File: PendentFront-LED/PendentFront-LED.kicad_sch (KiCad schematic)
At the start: 64 parts, among them J1 Conn_01x04_Pin, U1 74VHC9595FT, U2 74VHC9595FT, U3 74VHC9595FT

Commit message: Finalized pendent shape and started routing
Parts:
- removed J1: Conn_01x04_Pin, Connector_PinHeader_2.54mm:PinHeader_1x04_P2.54mm_Vertical, symbol Connector:Conn_01x04_Pin
- removed LED10, LED11, LED12, LED13, LED14, LED15, LED16, LED17, LED18, LED19, LED20, LED21, LED22, LED23, LED24, LED25, LED26, LED27, LED28, LED29, LED3, LED30, LED31, LED32, LED33, LED34, LED35, LED36, LED37, LED38, LED39, LED4, LED40, LED5, LED6, LED7, LED8, LED9: UHD111A-FKA-C3K23E1L3VG5ZB3Z3, PendentFrontFootprints:SMD4_UHD111A-FKA_CRW, symbol PendentFrontSymbols:UHD111A-FKA-C3K23E1L3VG5ZB3Z3
- added D10, D11, D12, D13, D14, D15, D16, D17, D18, D19, D2, D20, D21, D22, D23, D24, D25, D26, D27, D28, D29, D3, D30, D31, D32, D33, D34, D35, D36, D37, D38, D39, D4, D40, D41, D42, D43, D44, D45, D46, D47, D48, D49, D5, D50, D51, D52, D53, D54, D55, D56, D57, D58, D59, D6, D60, D61, D62, D63, D64, D7, D8: UHD111A-FKA-C3K23E1L3VG5ZB3Z3, SMD4_UHD111A-FKA_CRW, symbol PendentFrontSymbols:UHD111A-FKA-C3K23E1L3VG5ZB3Z3
- added J1: Conn_01x05_Pin, Connector_PinHeader_1.27mm:PinHeader_1x05_P1.27mm_Vertical, symbol Connector:Conn_01x05_Pin
- added R16, R17, R18, R19, R20, R21, R22, R23, R24: R, Resistor_SMD:R_0402_1005Metric_Pad0.72x0.64mm_HandSolder, symbol Device:R
- added U4: 74VHC9595FT, TSSOP16B_TOS, symbol PendentFrontSymbols:74VHC9595FT
- D1: renamed from LED1; footprint PendentFrontFootprints:SMD4_UHD111A-FKA_CRW -> SMD4_UHD111A-FKA_CRW
- D9: renamed from LED2; footprint PendentFrontFootprints:SMD4_UHD111A-FKA_CRW -> SMD4_UHD111A-FKA_CRW
- U1, U2, U3: footprint PendentFrontFootprints:TSSOP16B_TOS -> TSSOP16B_TOS
- renumbered LED41 to D65, R16 to R25
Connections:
- net AUX_LED: no longer U3.13 (Q8)
- net CLK: now also J1.2 (Pin_2), U4.3 (SCK), U4.4 (RCK)
- net COLOR.BLUE1: no longer U3.7 (Q3)
- net COLOR.BLUE2: no longer U3.9 (Q4)
- net COLOR.BLUE3: no longer U3.10 (Q5)
- net COLOR.BLUE4: no longer U3.11 (Q6)
- net COLOR.BLUE5: no longer U3.12 (Q7)
- net COLOR.GREEN1: no longer U2.11 (Q6)
- net COLOR.GREEN2: no longer U2.12 (Q7)
- net COLOR.GREEN3: no longer U2.13 (Q8)
- net COLOR.GREEN4: no longer U3.5 (Q1)
- net COLOR.GREEN5: no longer U3.6 (Q2)
- net COLOR.RED1: no longer U2.5 (Q1)
- net COLOR.RED2: no longer U2.6 (Q2)
- net COLOR.RED3: no longer U2.7 (Q3)
- net COLOR.RED4: no longer U2.9 (Q4)
- net COLOR.RED5: no longer U2.10 (Q5)
- net GND: now also J1.5 (Pin_5), U4.8 (GND)
- net SerialIn: now also J1.4 (Pin_4)
- net VCC: now also J1.1 (Pin_1), U4.1 (*SCLR), U4.16 (VCC)
- net at R13.1: now also D33.1, D34.1, D35.1, D36.1, D37.1, D38.1, D39.1, D40.1
- net at R14.1: now also D33.2, D34.2, D35.2, D36.2, D37.2, D38.2, D39.2, D40.2
- net at R15.1: now also D33.3, D34.3, D35.3, D36.3, D37.3, D38.3, D39.3, D40.3
- net at R10.1: now also D25.1, D26.1, D27.1, D28.1, D29.1, D30.1, D31.1, D32.1
- net at R11.1: now also D25.2, D26.2, D27.2, D28.2, D29.2, D30.2, D31.2, D32.2
- net at R12.1: now also D25.3, D26.3, D27.3, D28.3, D29.3, D30.3, D31.3, D32.3
- net at R7.1: now also D17.1, D18.1, D19.1, D20.1, D21.1, D22.1, D23.1, D24.1
- net at R8.1: now also D17.2, D18.2, D19.2, D20.2, D21.2, D22.2, D23.2, D24.2
- net at R9.1: now also D17.3, D18.3, D19.3, D20.3, D21.3, D22.3, D23.3, D24.3
- net at D1.1, R1.1: now also D2.1, D3.1, D4.1, D5.1, D6.1, D7.1, D8.1
- net at D1.2, R2.1: now also D2.2, D3.2, D4.2, D5.2, D6.2, D7.2, D8.2
- net at D1.3, R3.1: now also D2.3, D3.3, D4.3, D5.3, D6.3, D7.3, D8.3
- net at D9.1, R4.1: now also D10.1, D11.1, D12.1, D13.1, D14.1, D15.1, D16.1
- net at D9.2, R5.1: now also D10.2, D11.2, D12.2, D13.2, D14.2, D15.2, D16.2
- net at D9.3, R6.1: now also D10.3, D11.3, D12.3, D13.3, D14.3, D15.3, D16.3
- net at U3.15 (Q8C): now also U4.2 (SI)
- net COL1 renamed ROW1
- net ROW1: now also D17.4, D25.4, D33.4, D41.4, D49.4, D57.4; no longer U1.5 (Q1)
- net COL2: no longer names the net of U1.6 (Q2)
- net COL3: no longer names the net of U1.7 (Q3)
- net COL4: no longer names the net of U1.9 (Q4)
- net COL5: no longer names the net of U1.10 (Q5)
- net COL6: no longer names the net of U1.11 (Q6)
- net COL7: no longer names the net of U1.12 (Q7)
- net COL8: no longer names the net of U1.13 (Q8)
- new net: D57.1, D58.1, D59.1, D60.1, D61.1, D62.1, D63.1, D64.1, R22.1
- new net: D57.2, D58.2, D59.2, D60.2, D61.2, D62.2, D63.2, D64.2, R23.1
- new net: D57.3, D58.3, D59.3, D60.3, D61.3, D62.3, D63.3, D64.3, R24.1
- new net: D41.3, D42.3, D43.3, D44.3, D45.3, D46.3, D47.3, D48.3, R18.1
- new net: D49.1, D50.1, D51.1, D52.1, D53.1, D54.1, D55.1, D56.1, R19.1
- new net: D49.2, D50.2, D51.2, D52.2, D53.2, D54.2, D55.2, D56.2, R20.1
- new net: D49.3, D50.3, D51.3, D52.3, D53.3, D54.3, D55.3, D56.3, R21.1
- new net: D41.1, D42.1, D43.1, D44.1, D45.1, D46.1, D47.1, D48.1, R16.1
- new net: D41.2, D42.2, D43.2, D44.2, D45.2, D46.2, D47.2, D48.2, R17.1
- new net COLOR.BLUE6: R16.2
- new net COLOR.BLUE7: R19.2
- new net COLOR.BLUE8: R22.2
- new net COLOR.GREEN6: R17.2
- new net COLOR.GREEN7: R20.2
- new net COLOR.GREEN8: R23.2
- new net COLOR.RED6: R18.2
- new net COLOR.RED7: R21.2
- new net COLOR.RED8: R24.2
- new net RCK: J1.3 (Pin_3)
- new net ROW2: D10.4, D18.4, D2.4, D26.4, D34.4, D42.4, D50.4, D58.4
- new net ROW3: D11.4, D19.4, D27.4, D3.4, D35.4, D43.4, D51.4, D59.4
- new net ROW4: D12.4, D20.4, D28.4, D36.4, D4.4, D44.4, D52.4, D60.4
- new net ROW5: D13.4, D21.4, D29.4, D37.4, D45.4, D5.4, D53.4, D61.4
- new net ROW6: D14.4, D22.4, D30.4, D38.4, D46.4, D54.4, D6.4, D62.4
- new net ROW7: D15.4, D23.4, D31.4, D39.4, D47.4, D55.4, D63.4, D7.4
- new net ROW8: D16.4, D24.4, D32.4, D40.4, D48.4, D56.4, D64.4, D8.4
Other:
- moved on the sheet: C1, C2, C3, D1, D65, D9, R1, R2, R25, R3, U1, U2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

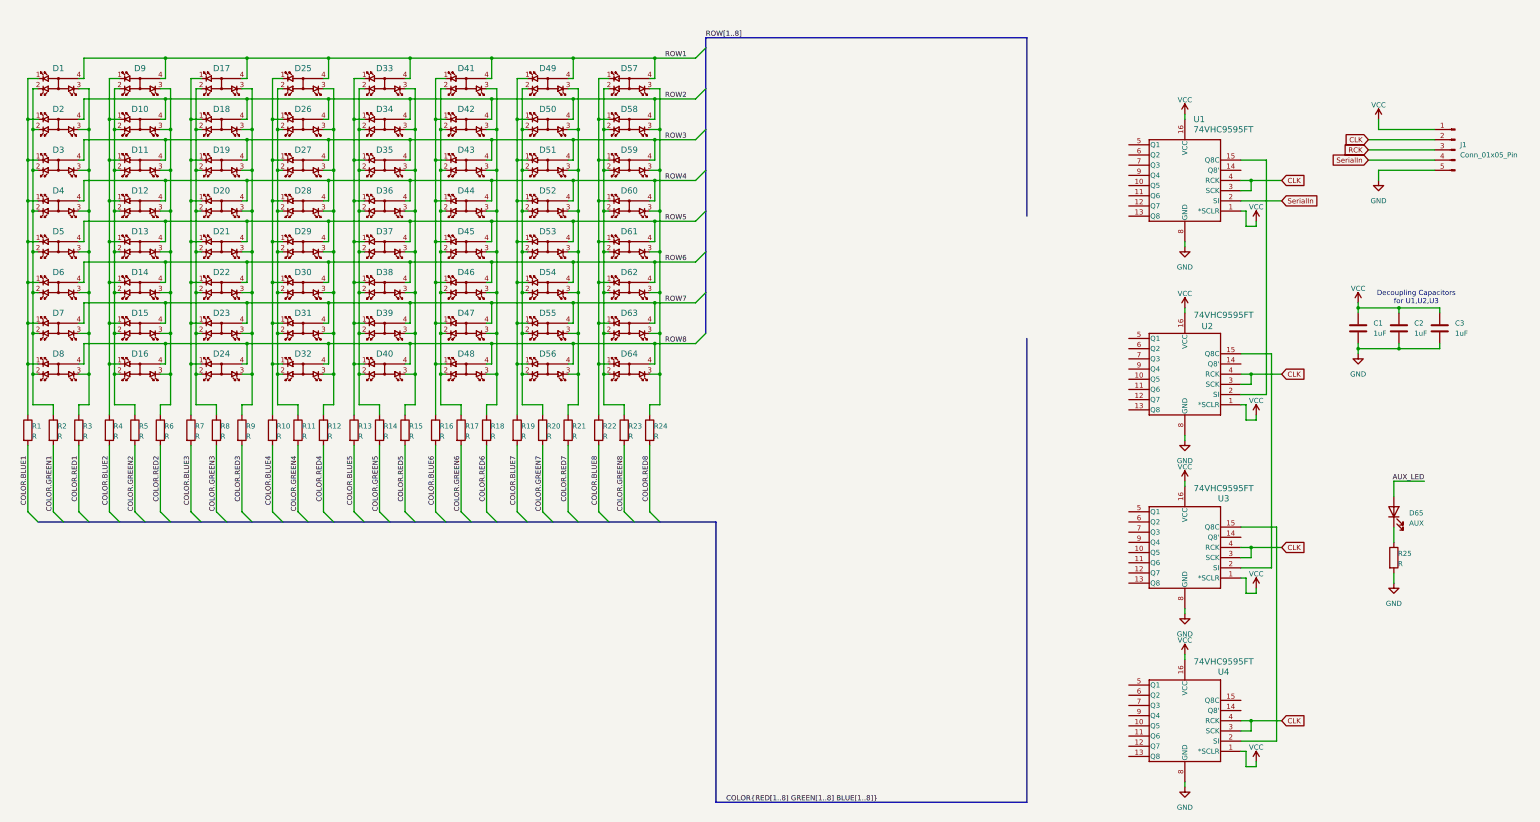
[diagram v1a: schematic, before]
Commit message: Connected up shift registers. Still need to rearrange connections to make routing possible
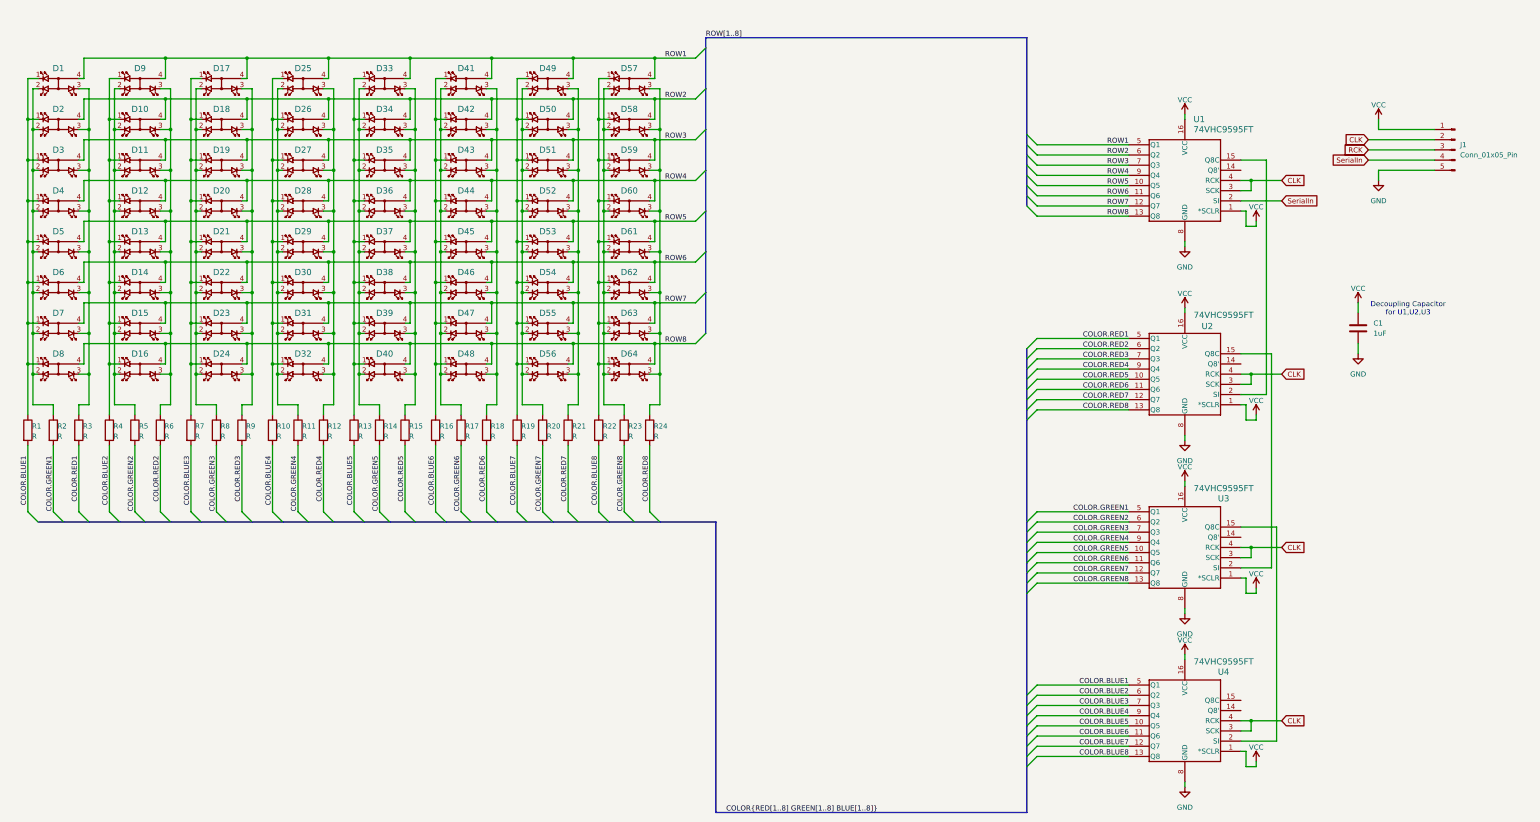
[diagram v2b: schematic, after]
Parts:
- removed C2, C3: 1uF, Capacitor_SMD:C_0402_1005Metric_Pad0.74x0.62mm_HandSolder, symbol Device:C
- removed D65: AUX, LED_SMD:LED_1206_3216Metric_Pad1.42x1.75mm_HandSolder, symbol Device:LED
- removed R25: R, Resistor_SMD:R_0402_1005Metric_Pad0.72x0.64mm_HandSolder, symbol Device:R
- D1, D10, D11, D12, D13, D14, D15, D16, D17, D18, D19, D2, D20, D21, D22, D23, D24, D25, D26, D27, D28, D29, D3, D30, D31, D32, D33, D34, D35, D36, D37, D38, D39, D4, D40, D41, D42, D43, D44, D45, D46, D47, D48, D49, D5, D50, D51, D52, D53, D54, D55, D56, D57, D58, D59, D6, D60, D61, D62, D63, D64, D7, D8, D9: footprint SMD4_UHD111A-FKA_CRW -> PendentFrontFootprints:SMD4_UHD111A-FKA_CRW
- R1, R10, R11, R12, R13, R14, R15, R16, R17, R18, R19, R2, R20, R21, R22, R23, R24, R3, R4, R5, R6, R7, R8, R9: footprint Resistor_SMD:R_0402_1005Metric_Pad0.72x0.64mm_HandSolder -> Resistor_SMD:R_0402_1005Metric
- U1, U2, U3, U4: footprint TSSOP16B_TOS -> PendentFrontFootprints:TSSOP16B_TOS
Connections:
- net COLOR.BLUE1: now also U4.5 (Q1)
- net COLOR.BLUE2: now also U4.6 (Q2)
- net COLOR.BLUE3: now also U4.7 (Q3)
- net COLOR.BLUE4: now also U4.9 (Q4)
- net COLOR.BLUE5: now also U4.10 (Q5)
- net COLOR.BLUE6: now also U4.11 (Q6)
- net COLOR.BLUE7: now also U4.12 (Q7)
- net COLOR.BLUE8: now also U4.13 (Q8)
- net COLOR.GREEN1: now also U3.5 (Q1)
- net COLOR.GREEN2: now also U3.6 (Q2)
- net COLOR.GREEN3: now also U3.7 (Q3)
- net COLOR.GREEN4: now also U3.9 (Q4)
- net COLOR.GREEN5: now also U3.10 (Q5)
- net COLOR.GREEN6: now also U3.11 (Q6)
- net COLOR.GREEN7: now also U3.12 (Q7)
- net COLOR.GREEN8: now also U3.13 (Q8)
- net COLOR.RED1: now also U2.5 (Q1)
- net COLOR.RED2: now also U2.6 (Q2)
- net COLOR.RED3: now also U2.7 (Q3)
- net COLOR.RED4: now also U2.9 (Q4)
- net COLOR.RED5: now also U2.10 (Q5)
- net COLOR.RED6: now also U2.11 (Q6)
- net COLOR.RED7: now also U2.12 (Q7)
- net COLOR.RED8: now also U2.13 (Q8)
- net ROW1: now also U1.5 (Q1)
- net ROW2: now also U1.6 (Q2)
- net ROW3: now also U1.7 (Q3)
- net ROW4: now also U1.9 (Q4)
- net ROW5: now also U1.10 (Q5)
- net ROW6: now also U1.11 (Q6)
- net ROW7: now also U1.12 (Q7)
- net ROW8: now also U1.13 (Q8)
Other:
- note added: "Decoupling Capacitor for U1,U2,U3"
- note removed: "Decoupling Capacitors for U1,U2,U3"

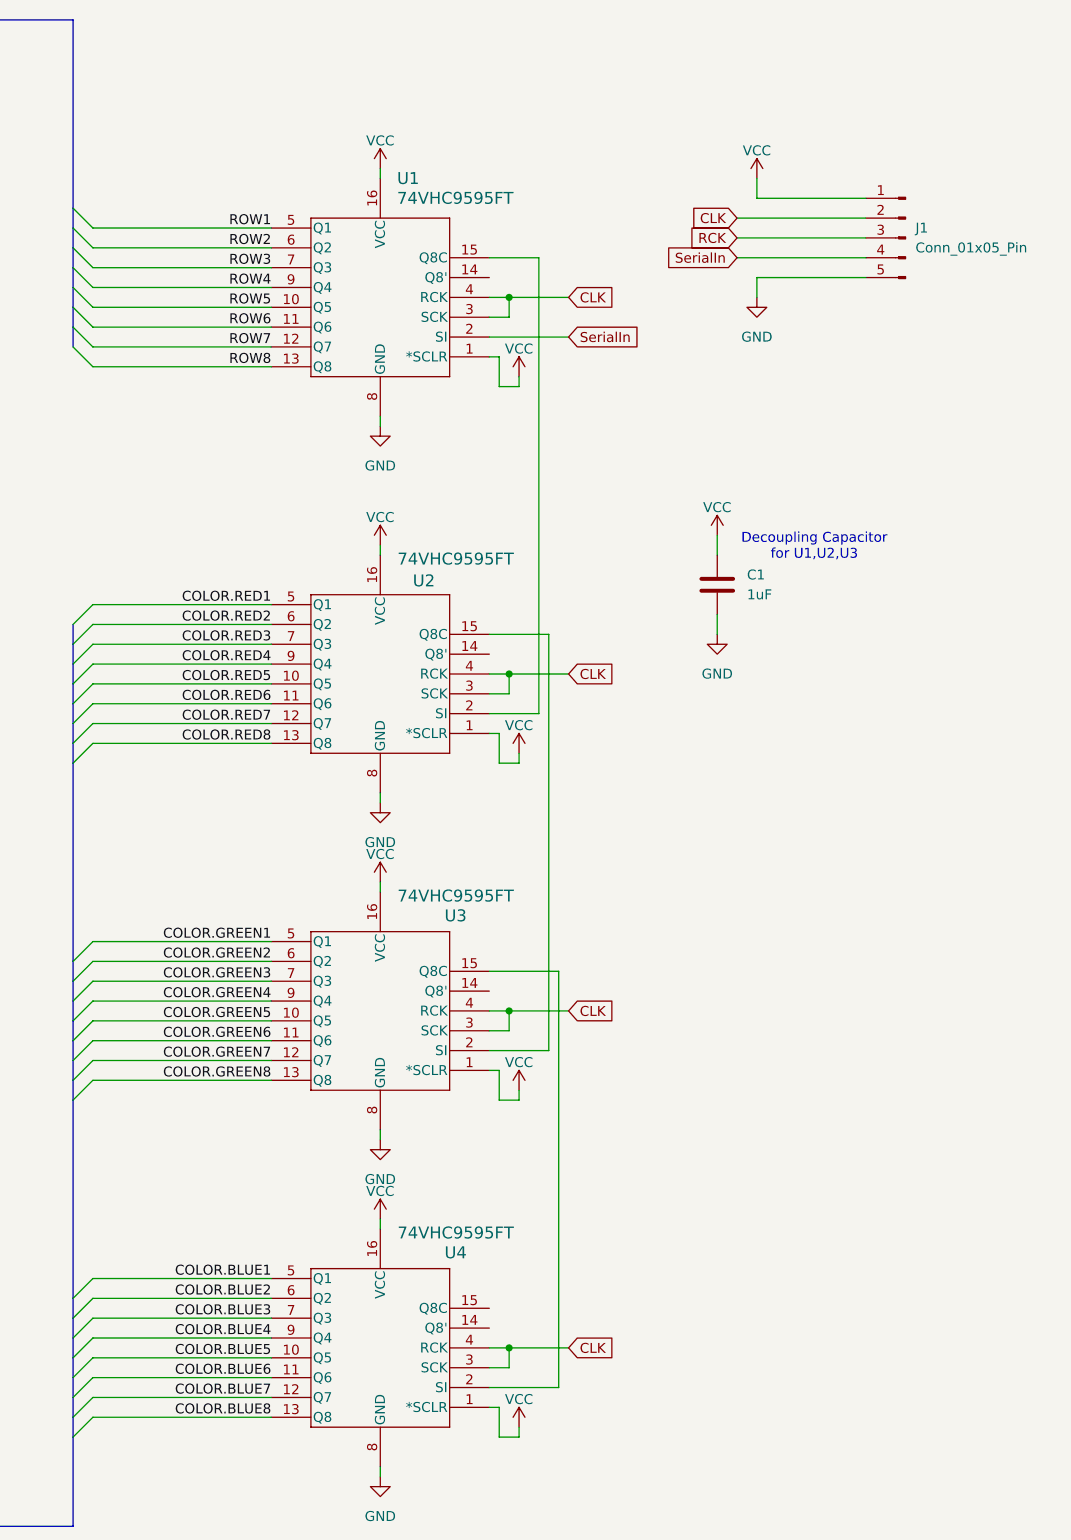
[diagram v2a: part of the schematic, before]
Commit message: More work on routing the front LED panel
Got through 2 1/2 groups of LEDs and reconfigured connections to shift registers to make routing easier. Split header into 2 groups for easier placement
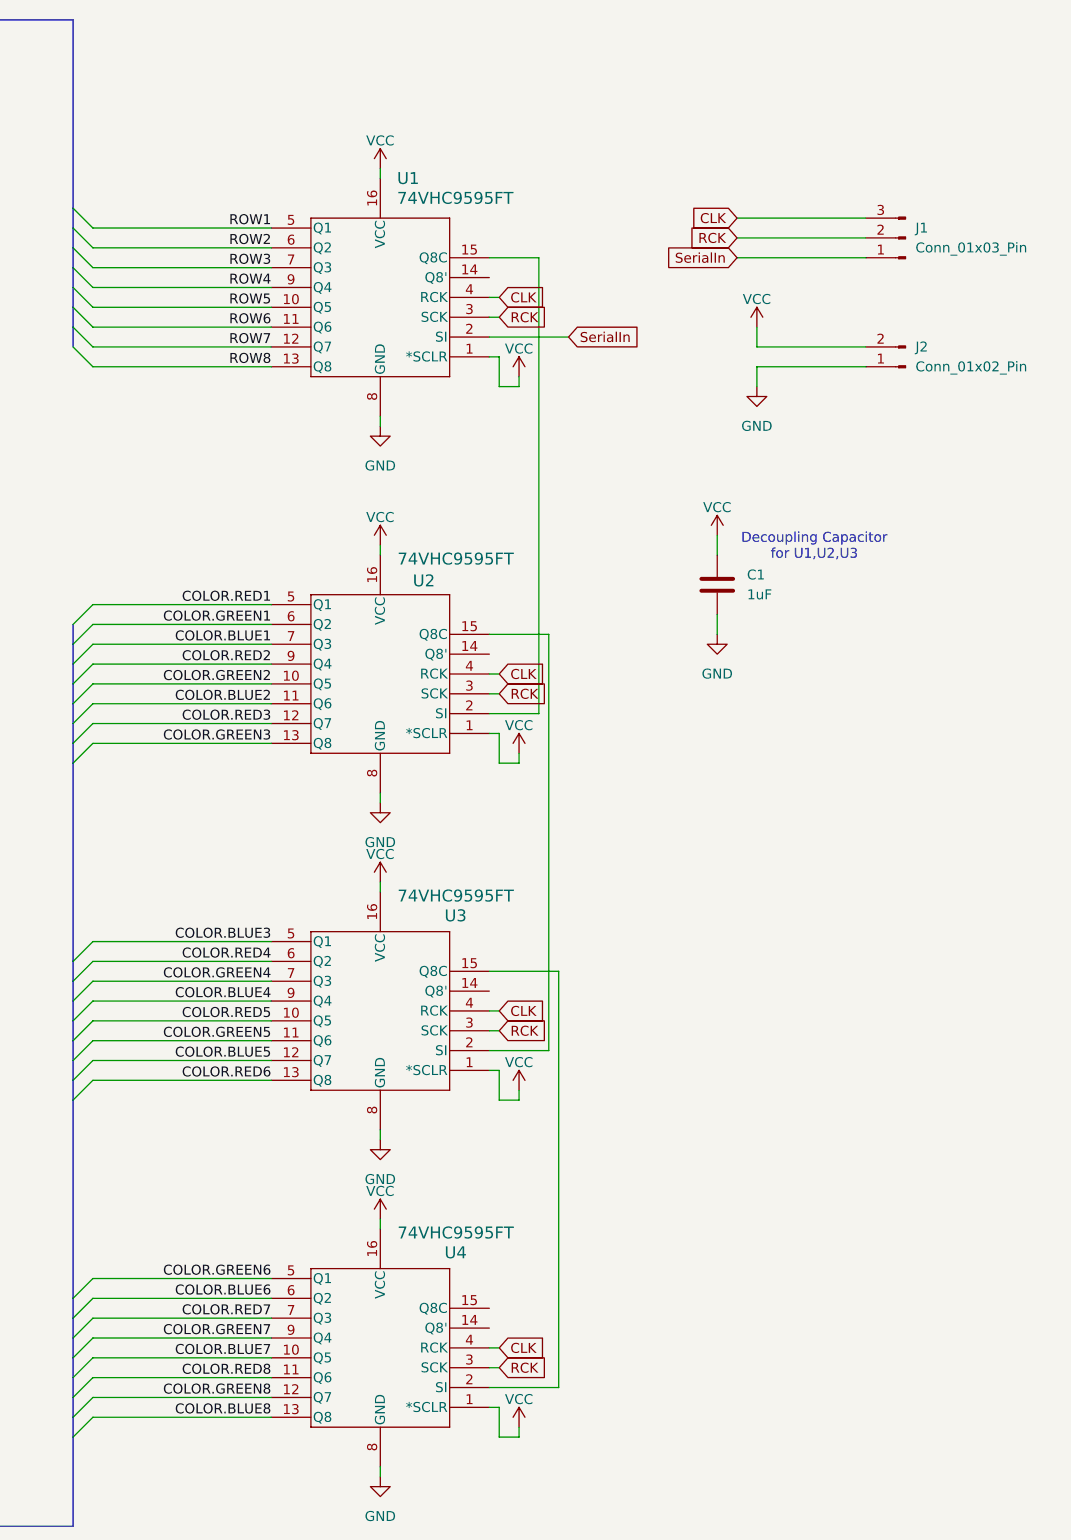
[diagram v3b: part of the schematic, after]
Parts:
- removed J1: Conn_01x05_Pin, Connector_PinHeader_1.27mm:PinHeader_1x05_P1.27mm_Vertical, symbol Connector:Conn_01x05_Pin
- added J1: Conn_01x03_Pin, Connector_PinHeader_1.27mm:PinHeader_1x03_P1.27mm_Vertical, symbol Connector:Conn_01x03_Pin
- added J2: Conn_01x02_Pin, Connector_PinHeader_1.27mm:PinHeader_1x02_P1.27mm_Vertical, symbol Connector:Conn_01x02_Pin
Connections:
- net CLK: now also J1.3 (Pin_3); no longer U1.3 (SCK), U2.3 (SCK), U3.3 (SCK), U4.3 (SCK)
- net COLOR.BLUE1: now also U2.7 (Q3); no longer U4.5 (Q1)
- net COLOR.BLUE2: now also U2.11 (Q6); no longer U4.6 (Q2)
- net COLOR.BLUE3: now also U3.5 (Q1); no longer U4.7 (Q3)
- net COLOR.BLUE4: now also U3.9 (Q4); no longer U4.9 (Q4)
- net COLOR.BLUE5: now also U3.12 (Q7); no longer U4.10 (Q5)
- net COLOR.BLUE6: now also U4.6 (Q2); no longer U4.11 (Q6)
- net COLOR.BLUE7: now also U4.10 (Q5); no longer U4.12 (Q7)
- net COLOR.GREEN1: now also U2.6 (Q2); no longer U3.5 (Q1)
- net COLOR.GREEN2: now also U2.10 (Q5); no longer U3.6 (Q2)
- net COLOR.GREEN3: now also U2.13 (Q8); no longer U3.7 (Q3)
- net COLOR.GREEN4: now also U3.7 (Q3); no longer U3.9 (Q4)
- net COLOR.GREEN5: now also U3.11 (Q6); no longer U3.10 (Q5)
- net COLOR.GREEN6: now also U4.5 (Q1); no longer U3.11 (Q6)
- net COLOR.GREEN7: now also U4.9 (Q4); no longer U3.12 (Q7)
- net COLOR.GREEN8: now also U4.12 (Q7); no longer U3.13 (Q8)
- net COLOR.RED2: now also U2.9 (Q4); no longer U2.6 (Q2)
- net COLOR.RED3: now also U2.12 (Q7); no longer U2.7 (Q3)
- net COLOR.RED4: now also U3.6 (Q2); no longer U2.9 (Q4)
- net COLOR.RED5: now also U3.10 (Q5); no longer U2.10 (Q5)
- net COLOR.RED6: now also U3.13 (Q8); no longer U2.11 (Q6)
- net COLOR.RED7: now also U4.7 (Q3); no longer U2.12 (Q7)
- net COLOR.RED8: now also U4.11 (Q6); no longer U2.13 (Q8)
- net GND: now also J2.1 (Pin_1)
- net RCK: now also U1.3 (SCK), U2.3 (SCK), U3.3 (SCK), U4.3 (SCK), J1.2 (Pin_2)
- net SerialIn: now also J1.1 (Pin_1)
- net VCC: now also J2.2 (Pin_2)
